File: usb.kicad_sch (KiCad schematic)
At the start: 6 parts, among them J1 USB_C_Receptacle_USB2.0, J17 USB_A, SW3 SW_USB, U2 MSUSB30

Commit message: Rev 1
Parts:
- added JP4: JP_USB_SWITCH, Jumper:SolderJumper-2_P1.3mm_Bridged_RoundedPad1.0x1.5mm, symbol Jumper:Jumper_2_Bridged
- added R11: 100K, Resistor_SMD:R_0603_1608Metric, symbol Device:R_Small
- J1: LCSC C319148 -> C165948
- renumbered J17 to J18
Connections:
- net at SW3.2 (B): now also R11.1; no longer U2.1 (S)
- net +3V3 renamed +3.3V
- new net: JP4.1 (A), R11.2, U2.1 (S)
- new net SWITCH: JP4.2 (B)

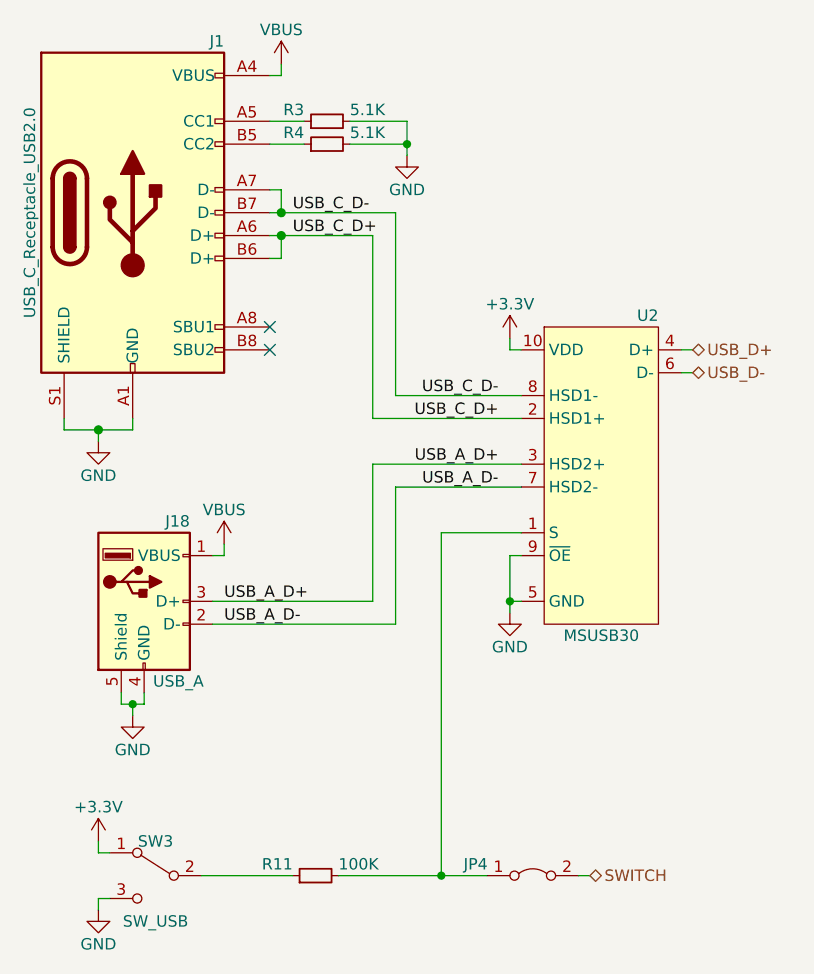
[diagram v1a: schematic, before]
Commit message: Rev 3
- USB Switch jumper open by default
- Power USB Host from 5V not VBUS
- Fix SPI pin silkscreen
- Add test points for USB D+/D-
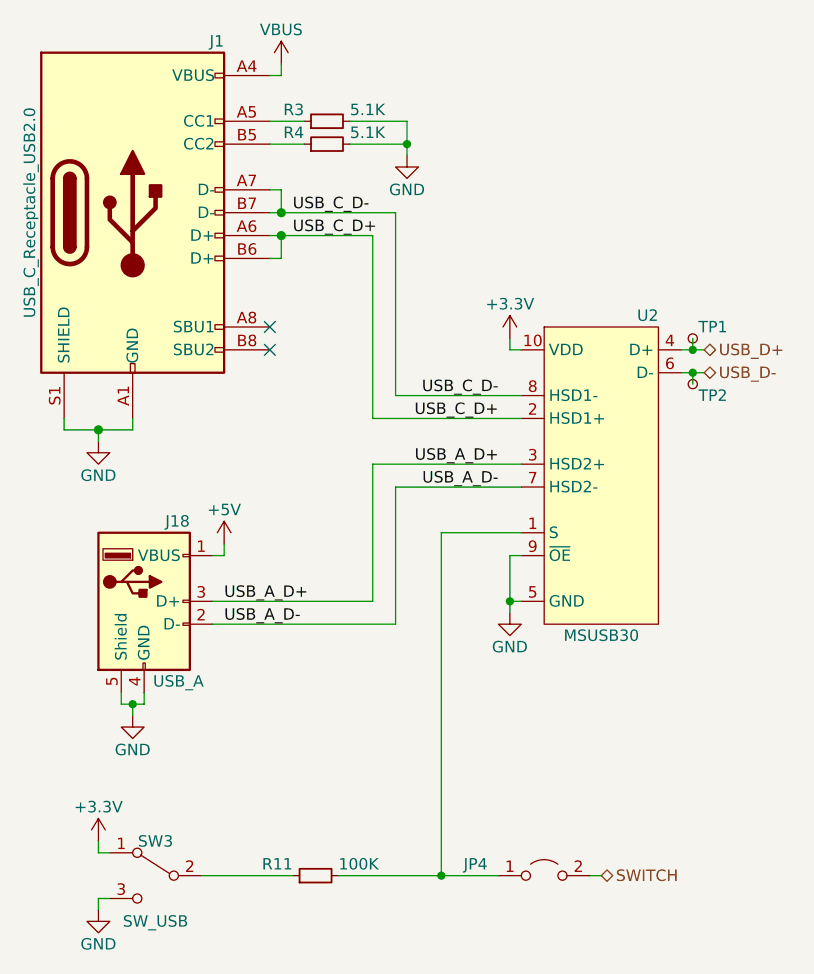
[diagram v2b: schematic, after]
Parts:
- added TP1: TP_USB_D+, TestPoint:TestPoint_Pad_D1.5mm, symbol Connector:TestPoint_Small
- added TP2: TP_USB_D-, TestPoint:TestPoint_Pad_D1.5mm, symbol Connector:TestPoint_Small
- JP4: footprint Jumper:SolderJumper-2_P1.3mm_Bridged_RoundedPad1.0x1.5mm -> Jumper:SolderJumper-2_P1.3mm_Open_RoundedPad1.0x1.5mm; symbol Jumper:Jumper_2_Bridged -> Jumper:Jumper_2_Open
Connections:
- net USB_D+: now also TP1.1
- net USB_D-: now also TP2.1
- net VBUS: no longer J18.1 (VBUS)
- new net +5V: J18.1 (VBUS)
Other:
- moved on the sheet: JP4
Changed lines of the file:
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@@
+	)
+	(junction
+		(at 177.8 85.09)
+		(diameter 0)
+		(color 0 0 0 0)
 	)
 	(junction
@@
 	)
 	(junction
+		(at 177.8 82.55)
+		(diameter 0)
+		(color 0 0 0 0)
+	)
+	(junction
 		(at 132.08 67.31)
 		(diameter 1.016)
@@
 	(wire
 		(pts
-			(xy 166.37 140.97) (xy 165.1 140.97)
+			(xy 167.64 140.97) (xy 166.37 140.97)
 		)
 		(stroke
@@
 	(wire
 		(pts
+			(xy 177.8 85.09) (xy 177.8 86.36)
+		)
+		(stroke
+			(width 0)
+			(type default)
+		)
+	)
+	(wire
+		(pts
 			(xy 157.48 81.28) (xy 157.48 82.55)
 		)
@@
 	(wire
 		(pts
+			(xy 177.8 85.09) (xy 179.07 85.09)
+		)
+		(stroke
+			(width 0)
+			(type default)
+		)
+	)
+	(wire
+		(pts
+			(xy 177.8 81.28) (xy 177.8 82.55)
+		)
+		(stroke
+			(width 0)
+			(type default)
+		)
+	)
+	(wire
+		(pts
 			(xy 132.08 67.31) (xy 144.78 67.31)
 		)
@@
 	(wire
 		(pts
+			(xy 177.8 82.55) (xy 179.07 82.55)
+		)
+		(stroke
+			(width 0)
+			(type default)
+		)
+	)
+	(wire
+		(pts
 			(xy 115.57 121.92) (xy 116.84 121.92)
 		)
@@
 	(wire
 		(pts
-			(xy 149.86 140.97) (xy 154.94 140.97)
+			(xy 149.86 140.97) (xy 156.21 140.97)
 		)
 		(stroke
@@
 	(hierarchical_label "USB_D+"
 		(shape bidirectional)
-		(at 177.8 82.55 0)
+		(at 179.07 82.55 0)
 		(fields_autoplaced yes)
 		(effects
@@
 	(hierarchical_label "USB_D-"
 		(shape bidirectional)
-		(at 177.8 85.09 0)
+		(at 179.07 85.09 0)
 		(fields_autoplaced yes)
 		(effects
@@
 	(hierarchical_label "SWITCH"
 		(shape bidirectional)
-		(at 166.37 140.97 0)
+		(at 167.64 140.97 0)
 		(fields_autoplaced yes)
 		(effects
@@
 	)
 	(symbol
+		(lib_id "Connector:TestPoint_Small")
+		(at 177.8 86.36 180)
+		(unit 1)
+		(exclude_from_sim no)
+		(in_bom yes)
+		(on_board yes)
+		(dnp no)
+		(property "Reference" "TP2"
+			(at 178.435 87.63 0)
+			(effects
+				(font
+					(size 1.27 1.27)
+				)
+				(justify right)
+			)
+		)
+		(property "Value" "TP_USB_D-"
+			(at 176.53 85.0901 0)
+			(effects
+				(font
+					(size 1.27 1.27)
+				)
+				(justify left)
+				(hide yes)
+			)
+		)
+		(property "Footprint" "TestPoint:TestPoint_Pad_D1.5mm"
+			(at 172.72 86.36 0)
+			(effects
+				(font
+					(size 1.27 1.27)
+				)
+				(hide yes)
+			)
+		)
+		(property "Datasheet" "~"
+			(at 172.72 86.36 0)
+			(effects
+				(font
+					(size 1.27 1.27)
+				)
+				(hide yes)
+			)
+		)
+		(property "Description" "test point"
+			(at 177.8 86.36 0)
+			(effects
+				(font
+					(size 1.27 1.27)
+				)
+				(hide yes)
+			)
+		)
+		(pin "1"
+		)
+		(instances
+			(project "rp2xxx_stamp_carrier"
+				(path "/7dc57191-1ee2-4888-98f8-9f12d0d1da37/ad4040ae-0da1-4e97-af65-b9c935f098a2"
+					(reference "TP2")
+					(unit 1)
+				)
+			)
+		)
+	)
+	(symbol
 		(lib_id "Interface_USB_Extra:MSUSB30")
 		(at 167.64 97.79 0)
@@
 	)
 	(symbol
-		(lib_id "power:VBUS")
+		(lib_id "Jumper:Jumper_2_Open")
+		(at 161.29 140.97 0)
+		(unit 1)
+		(exclude_from_sim no)
+		(in_bom yes)
+		(on_board yes)
+		(dnp no)
+		(property "Reference" "JP4"
+			(at 153.67 139.7 0)
+			(effects
+				(font
+					(size 1.27 1.27)
+				)
+			)
+		)
+		(property "Value" "JP_USB_SWITCH"
+			(at 161.29 138.43 0)
+			(effects
+				(font
+					(size 1.27 1.27)
+				)
+				(hide yes)
+			)
+		)
+		(property "Footprint" "Jumper:SolderJumper-2_P1.3mm_Open_RoundedPad1.0x1.5mm"
+			(at 161.29 140.97 0)
+			(effects
+				(font
+					(size 1.27 1.27)
+				)
+				(hide yes)
+			)
+		)
+		(property "Datasheet" "~"
+			(at 161.29 140.97 0)
+			(effects
+				(font
+					(size 1.27 1.27)
+				)
+				(hide yes)
+			)
+		)
+		(property "Description" "Jumper, 2-pole, closed/bridged"
+			(at 161.29 140.97 0)
+			(effects
+				(font
+					(size 1.27 1.27)
+				)
+				(hide yes)
+			)
+		)
+		(pin "2"
+		)
+		(pin "1"
+		)
+		(instances
+			(project "rp2xxx_stamp_carrier"
+				(path "/7dc57191-1ee2-4888-98f8-9f12d0d1da37/ad4040ae-0da1-4e97-af65-b9c935f098a2"
+					(reference "JP4")
+					(unit 1)
+				)
+			)
+		)
+	)
+	(symbol
+		(lib_id "power:+5V")
 		(at 125.73 104.14 0)
 		(unit 1)
@@
 		(dnp no)
 		(fields_autoplaced yes)
-		(property "Reference" "#PWR0118"
+		(property "Reference" "#PWR051"
 			(at 127 102.87 0)
 			(effects
@@
 			)
 		)
-		(property "Value" "VBUS"
+		(property "Value" "+5V"
 			(at 125.73 100.33 0)
 			(effects
@@
 			)
 		)
-		(property "Description" "Power symbol creates a global label with name \"VBUS\""
+		(property "Description" "Power symbol creates a global label with name \"+5V\""
 			(at 125.73 104.14 0)
 			(effects
@@
 				(hide yes)
 			)
-		)
-		(pin "1"
-		)
-		(instances
-			(project "rp2040_stamp_carrier"
-				(path "/5b7c14af-0dec-4110-816c-7b17205e8ed2"
-					(reference "#PWR0118")
-					(unit 1)
-				)
-			)
-			(project "rp2xxx_stamp_carrier"
-				(path "/7dc57191-1ee2-4888-98f8-9f12d0d1da37/ad4040ae-0da1-4e97-af65-b9c935f098a2"
-					(reference "#PWR0106")
-					(unit 1)
-				)
-			)
-		)
-	)
-	(symbol
-		(lib_id "Jumper:Jumper_2_Bridged")
-		(at 160.02 140.97 0)
-		(unit 1)
-		(exclude_from_sim no)
-		(in_bom yes)
-		(on_board yes)
-		(dnp no)
-		(property "Reference" "JP4"
-			(at 153.67 139.7 0)
-			(effects
-				(font
-					(size 1.27 1.27)
-				)
-			)
-		)
-		(property "Value" "JP_USB_SWITCH"
-			(at 160.02 138.43 0)
-			(effects
-				(font
-					(size 1.27 1.27)
-				)
-				(hide yes)
-			)
-		)
-		(property "Footprint" "Jumper:SolderJumper-2_P1.3mm_Bridged_RoundedPad1.0x1.5mm"
-			(at 160.02 140.97 0)
-			(effects
-				(font
-					(size 1.27 1.27)
-				)
-				(hide yes)
-			)
-		)
-		(property "Datasheet" "~"
-			(at 160.02 140.97 0)
-			(effects
-				(font
-					(size 1.27 1.27)
-				)
-				(hide yes)
-			)
-		)
-		(property "Description" "Jumper, 2-pole, closed/bridged"
-			(at 160.02 140.97 0)
-			(effects
-				(font
-					(size 1.27 1.27)
-				)
-				(hide yes)
-			)
-		)
-		(pin "2"
 		)
 		(pin "1"
@@
 			(project "rp2xxx_stamp_carrier"
 				(path "/7dc57191-1ee2-4888-98f8-9f12d0d1da37/ad4040ae-0da1-4e97-af65-b9c935f098a2"
-					(reference "JP4")
+					(reference "#PWR051")
 					(unit 1)
 				)
@@
 					(unit 1)
 				)
+			)
+		)
+	)
+	(symbol
+		(lib_id "Connector:TestPoint_Small")
+		(at 177.8 81.28 0)
+		(unit 1)
+		(exclude_from_sim no)
+		(in_bom yes)
+		(on_board yes)
+		(dnp no)
+		(property "Reference" "TP1"
+			(at 178.435 80.01 0)
+			(effects
+				(font
+					(size 1.27 1.27)
+				)
+				(justify left)
+			)
+		)
+		(property "Value" "TP_USB_D+"
+			(at 179.07 82.5499 0)
+			(effects
+				(font
+					(size 1.27 1.27)
+				)
+				(justify left)
+				(hide yes)
+			)
+		)
+		(property "Footprint" "TestPoint:TestPoint_Pad_D1.5mm"
+			(at 182.88 81.28 0)
+			(effects
+				(font
+					(size 1.27 1.27)
+				)
+				(hide yes)
+			)
+		)
+		(property "Datasheet" "~"
+			(at 182.88 81.28 0)
+			(effects
+				(font
+					(size 1.27 1.27)
+				)
+				(hide yes)
+			)
+		)
+		(property "Description" "test point"
+			(at 177.8 81.28 0)
+			(effects
+				(font
+					(size 1.27 1.27)
+				)
+				(hide yes)
+			)
+		)
+		(pin "1"
+		)
+		(instances
+			(project ""
+				(path "/7dc57191-1ee2-4888-98f8-9f12d0d1da37/ad4040ae-0da1-4e97-af65-b9c935f098a2"
+					(reference "TP1")
+					(unit 1)
+				)

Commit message: Rev 3.1, add README, and LICENSE
- Fixed the microSD pin silkscreen
- Updated BOM
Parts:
- TP1, TP2: now left out of the parts list
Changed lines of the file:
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@@
 		(unit 1)
 		(exclude_from_sim no)
-		(in_bom yes)
+		(in_bom no)
 		(on_board yes)
 		(dnp no)
@@
 			)
 		)
-		(property "Description" "test point"
+		(property "Description" ""
 			(at 177.8 86.36 0)
 			(effects
@@
 			)
 		)
-		(property "Description" "Jumper, 2-pole, closed/bridged"
+		(property "Description" ""
 			(at 161.29 140.97 0)
 			(effects
@@
 			)
 		)
-		(property "Description" "USB Type A connector"
+		(property "Description" ""
 			(at 116.84 110.49 0)
 			(effects
@@
 		(unit 1)
 		(exclude_from_sim no)
-		(in_bom yes)
+		(in_bom no)
 		(on_board yes)
 		(dnp no)
@@
 			)
 		)
-		(property "Description" "test point"
+		(property "Description" ""
 			(at 177.8 81.28 0)
 			(effects
@@
 			)
 		)
-		(property "Description" "Switch, single pole double throw"
+		(property "Description" ""
 			(at 118.11 140.97 0)
 			(effects
